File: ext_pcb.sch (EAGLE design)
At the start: 38 parts, among them CN10 MCV_05/4-G-2,5V, CN11 MCV_05/4-G-2,5V, CN12 MCV_05/4-G-2,5V, CN13 MCV_05/4-G-2,5V, CN15 MCV_05/2-G-2,5V, CN16 MCV_05/2-G-2,5V, CN17 MCV_05/2-G-2,5V, CN2 53047-08, CN3 53047-06, CN4 MCV_05/4-G-2,5V, CN5 53047-04, CN6 MCV_05/4-G-2,5V, CN7 MCV_05/4-G-2,5V, CN8 MCV_05/4-G-2,5V, CN9 MCV_05/6-G-2,5V, U1 LP298XS, U2 4049D

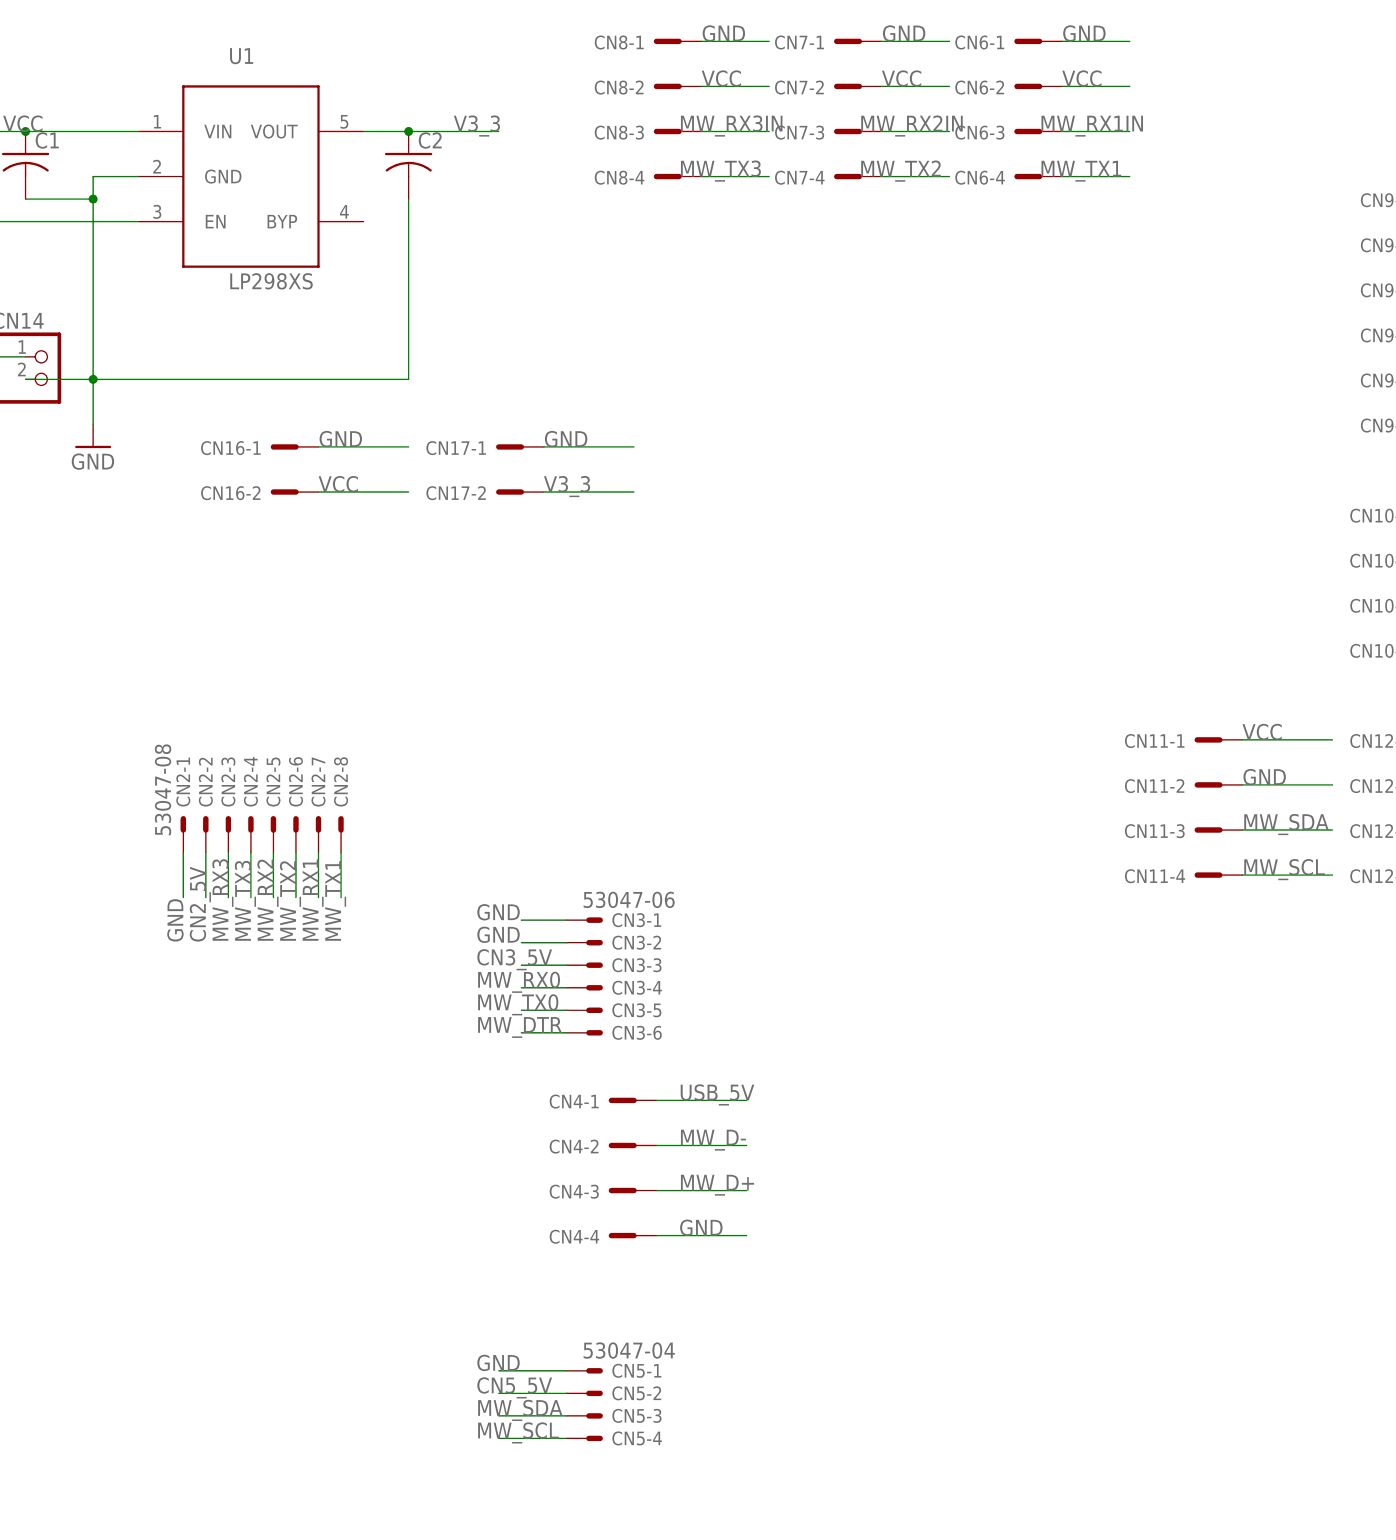
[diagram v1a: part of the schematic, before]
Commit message: Finish PCB traces
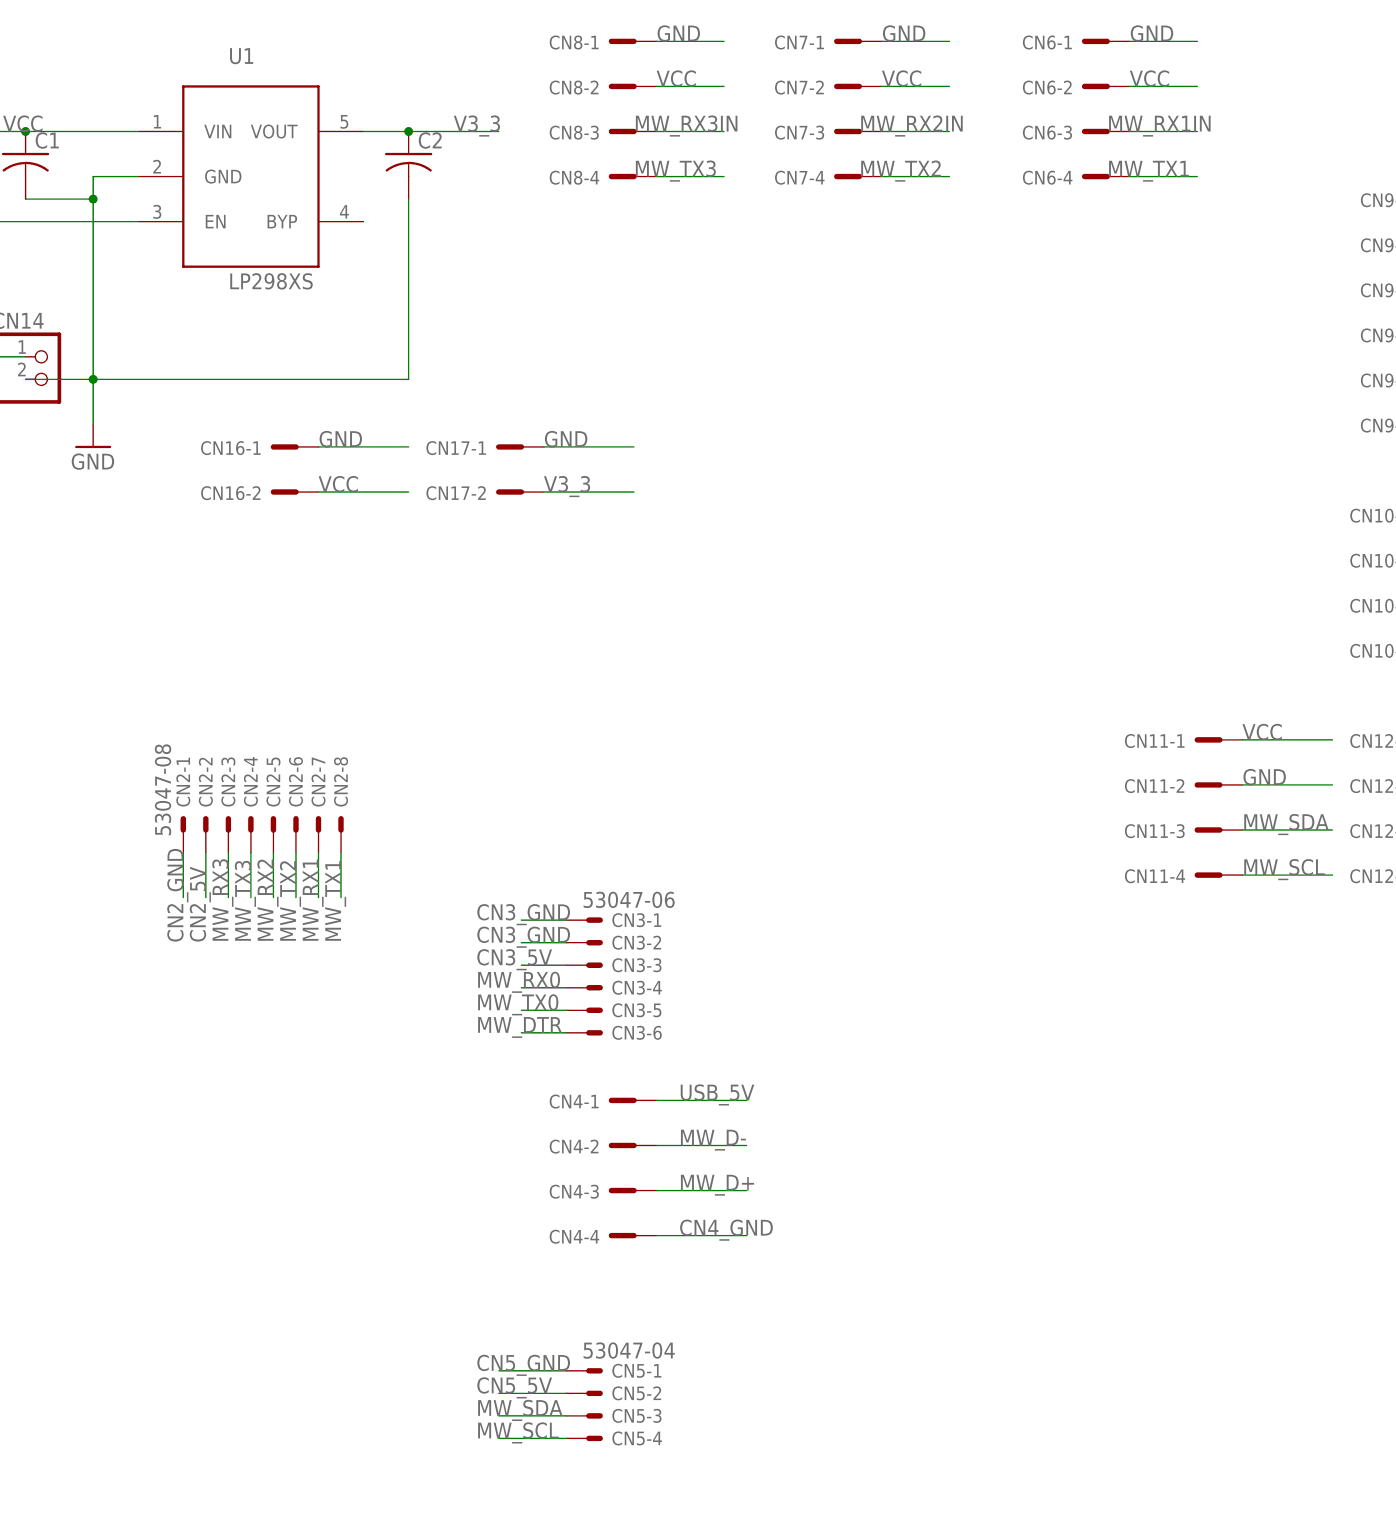
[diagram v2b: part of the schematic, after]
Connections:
- new net CN2_GND: CN2-1.S
- new net CN3_GND: CN3-1.S, CN3-2.S
- new net CN4_GND: CN4-4.SK
- new net CN5_GND: CN5-1.S
- net GND: no longer CN2-1.S, CN3-1.S, CN3-2.S, CN4-4.SK, CN5-1.S
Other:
- moved on the sheet: CN6-1, CN6-2, CN6-3, CN6-4, CN8-1, CN8-2, CN8-3, CN8-4
